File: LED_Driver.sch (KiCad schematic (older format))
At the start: 0 parts

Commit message: Understanding the LED Driver Module
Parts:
- added C? (x2): C, symbol C
- added D?: DIODESCH, symbol DIODESCH
- added L?: INDUCTOR, symbol INDUCTOR
- added R?: R, symbol R
- added U?: AP5726, symbol AP5726
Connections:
- net String+: now also C?.1, D?.2 (K), U?.5 (OVP)
- net String-: now also R?.1, U?.3 (FB)
- new net: D?.1 (A), L?.2, U?.1 (SW)
- new net +5V: C?.1, L?.1, U?.6 (VIN)
- new net GND: C?.2, C?.2, R?.2, U?.2 (GND)
- new net LED_EN_PWM: U?.4 (EN)
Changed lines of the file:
@@
 $Descr A4 11693 8268
 encoding utf-8
-Sheet 6 9
+Sheet 5 9
 Title ""
 Date ""
@@
 Comment4 ""
 $EndDescr
-Text HLabel 2350 2650 0    60   Input ~ 0
-EN
-Text HLabel 2350 3050 0    60   Input ~ 0
-FREQ
-Text HLabel 8650 2650 0    60   Output ~ 0
+Text HLabel 4400 3350 0    60   Input ~ 0
+LED_EN_PWM
+Text HLabel 8500 2100 2    60   Output ~ 0
 String+
-Text HLabel 8650 3000 0    60   Input ~ 0
+Text HLabel 8550 3500 2    60   Input ~ 0
 String-
+$Comp
+L AP5726 U?
+U 1 1 52F43ADC
+P 5400 3350
+F 0 "U?" H 5700 2900 60  0000 C CNN
+F 1 "AP5726" H 5400 3400 60  0000 C CNN
+F 2 "" H 5300 2750 60  0000 C CNN
+F 3 "" H 5300 2750 60  0000 C CNN
+	1    5400 3350
+	1    0    0    -1
+$EndComp
+$Comp
+L +5V #PWR?
+U 1 1 52F43D0D
+P 4550 1950
+F 0 "#PWR?" H 4550 2040 20  0001 C CNN
+F 1 "+5V" H 4550 2040 30  0000 C CNN
+F 2 "" H 4550 1950 60  0000 C CNN
+F 3 "" H 4550 1950 60  0000 C CNN
+	1    4550 1950
+	1    0    0    -1
+$EndComp
+$Comp
+L GND #PWR?
+U 1 1 52F43D24
+P -25900 -92000
+F 0 "#PWR?" H -25900 -92000 30  0001 C CNN
+F 1 "GND" H -25900 -92070 30  0001 C CNN
+F 2 "" H -25900 -92000 60  0000 C CNN
+F 3 "" H -25900 -92000 60  0000 C CNN
+	1    -25900 -92000
+	1    0    0    -1
+$EndComp
+$Comp
+L GND #PWR?
+U 1 1 52F43D42
+P 4550 2800
+F 0 "#PWR?" H 4550 2800 30  0001 C CNN
+F 1 "GND" H 4550 2730 30  0001 C CNN
+F 2 "" H 4550 2800 60  0000 C CNN
+F 3 "" H 4550 2800 60  0000 C CNN
+	1    4550 2800
+	1    0    0    -1
+$EndComp
+$Comp
+L GND #PWR?
+U 1 1 52F43D54
+P 5400 4500
+F 0 "#PWR?" H 5400 4500 30  0001 C CNN
+F 1 "GND" H 5400 4430 30  0001 C CNN
+F 2 "" H 5400 4500 60  0000 C CNN
+F 3 "" H 5400 4500 60  0000 C CNN
+	1    5400 4500
+	1    0    0    -1
+$EndComp
+$Comp
+L C C?
+U 1 1 52F43D64
+P 4550 2400
+F 0 "C?" H 4550 2500 40  0000 L CNN
+F 1 "C" H 4556 2315 40  0000 L CNN
+F 2 "" H 4588 2250 30  0000 C CNN
+F 3 "" H 4550 2400 60  0000 C CNN
+	1    4550 2400
+	1    0    0    -1
+$EndComp
+$Comp
+L C C?
+U 1 1 52F43D9A
+P 7650 2400
+F 0 "C?" H 7650 2500 40  0000 L CNN
+F 1 "C" H 7656 2315 40  0000 L CNN
+F 2 "" H 7688 2250 30  0000 C CNN
+F 3 "" H 7650 2400 60  0000 C CNN
+	1    7650 2400
+	1    0    0    -1
+$EndComp
+$Comp
+L INDUCTOR L?
+U 1 1 52F43DA7
+P 5400 1900
+F 0 "L?" V 5350 1900 40  0000 C CNN
+F 1 "INDUCTOR" V 5500 1900 40  0000 C CNN
+F 2 "" H 5400 1900 60  0000 C CNN
+F 3 "" H 5400 1900 60  0000 C CNN
+	1    5400 1900
+	0    -1   -1   0
+$EndComp
+$Comp
+L DIODESCH D?
+U 1 1 52F43DD1
+P 6050 2100
+F 0 "D?" H 6050 2200 40  0000 C CNN
+F 1 "DIODESCH" H 6050 2000 40  0000 C CNN
+F 2 "" H 6050 2100 60  0000 C CNN
+F 3 "" H 6050 2100 60  0000 C CNN
+	1    6050 2100
+	1    0    0    -1
+$EndComp
+$Comp
+L GND #PWR?
+U 1 1 52F43E01
+P 7650 2800
+F 0 "#PWR?" H 7650 2800 30  0001 C CNN
+F 1 "GND" H 7650 2730 30  0001 C CNN
+F 2 "" H 7650 2800 60  0000 C CNN
+F 3 "" H 7650 2800 60  0000 C CNN
+	1    7650 2800
+	1    0    0    -1
+$EndComp
+$Comp
+L R R?
+U 1 1 52F43E56
+P 6250 3900
+F 0 "R?" V 6330 3900 40  0000 C CNN
+F 1 "R" V 6257 3901 40  0000 C CNN
+F 2 "" V 6180 3900 30  0000 C CNN
+F 3 "" H 6250 3900 30  0000 C CNN
+	1    6250 3900
+	1    0    0    -1
+$EndComp
+Wire Wire Line
+	4400 3350 4650 3350
+Wire Wire Line
+	5400 4500 5400 4050
+Wire Wire Line
+	4550 2800 4550 2600
+Wire Wire Line
+	4550 1950 4550 2200
+Wire Wire Line
+	4550 2100 5250 2100
+Wire Wire Line
+	5250 2100 5250 2650
+Connection ~ 4550 2100
+Wire Wire Line
+	5100 1900 5100 2100
+Connection ~ 5100 2100
+Wire Wire Line
+	5550 2650 5550 2100
+Wire Wire Line
+	5550 2100 5850 2100
+Wire Wire Line
+	5700 2100 5700 1900
+Connection ~ 5700 2100
+Wire Wire Line
+	6250 2100 8500 2100
+Wire Wire Line
+	7650 2100 7650 2200
+Wire Wire Line
+	7650 2800 7650 2600
+Wire Wire Line
+	6100 3200 6350 3200
+Wire Wire Line
+	6350 3200 6350 2100
+Connection ~ 6350 2100
+Connection ~ 7650 2100
+Wire Wire Line
+	6100 3500 8550 3500
+Wire Wire Line
+	6250 3500 6250 3650
+Wire Wire Line
+	6250 4150 6250 4300
+Wire Wire Line
+	6250 4300 5400 4300
+Connection ~ 5400 4300
+Connection ~ 6250 3500
 $EndSCHEMATC

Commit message: Understanding the Arduino Module
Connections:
- net String+ renamed LED_STRING+
- net String- renamed LED_STRING-
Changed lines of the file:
@@
 LIBS:valves
 LIBS:MyComponents
+LIBS:arduino_shieldsNCL
 LIBS:BenchBuddy-cache
 EELAYER 24 0
@@
 LED_EN_PWM
 Text HLabel 8500 2100 2    60   Output ~ 0
-String+
-Text HLabel 8550 3500 2    60   Input ~ 0
-String-
+LED_STRING+
+Text HLabel 8550 3500 2    60   Output ~ 0
+LED_STRING-
 $Comp
 L AP5726 U?

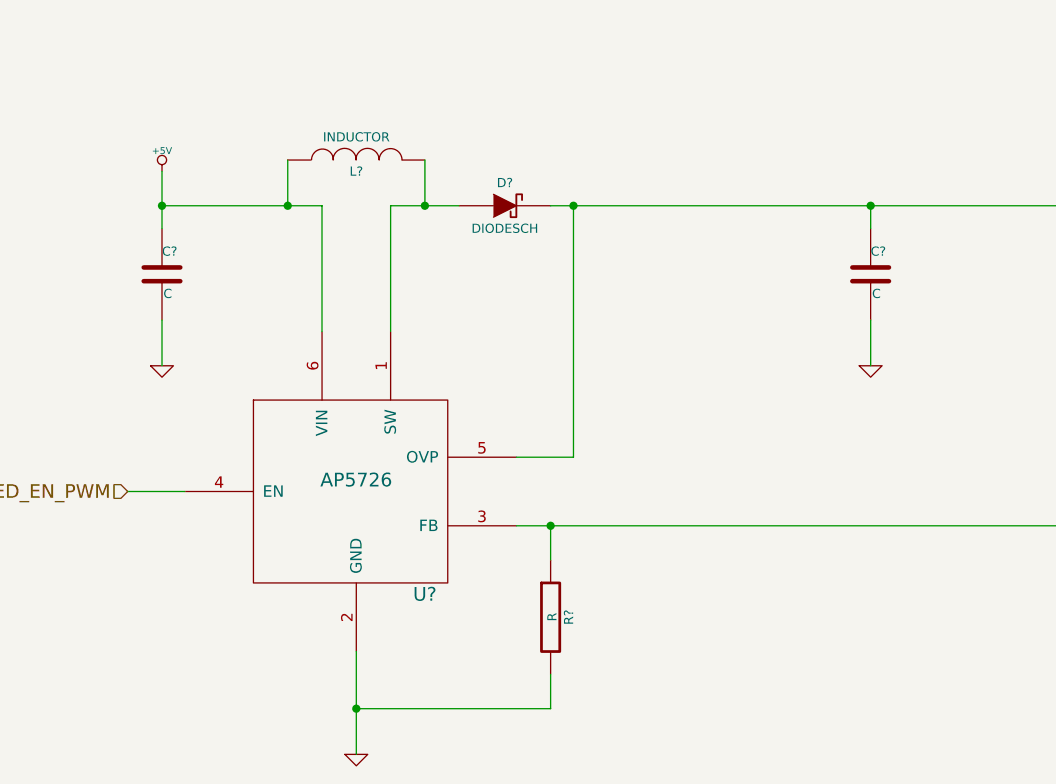
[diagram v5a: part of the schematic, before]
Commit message: Associating and Placing the Relay Module
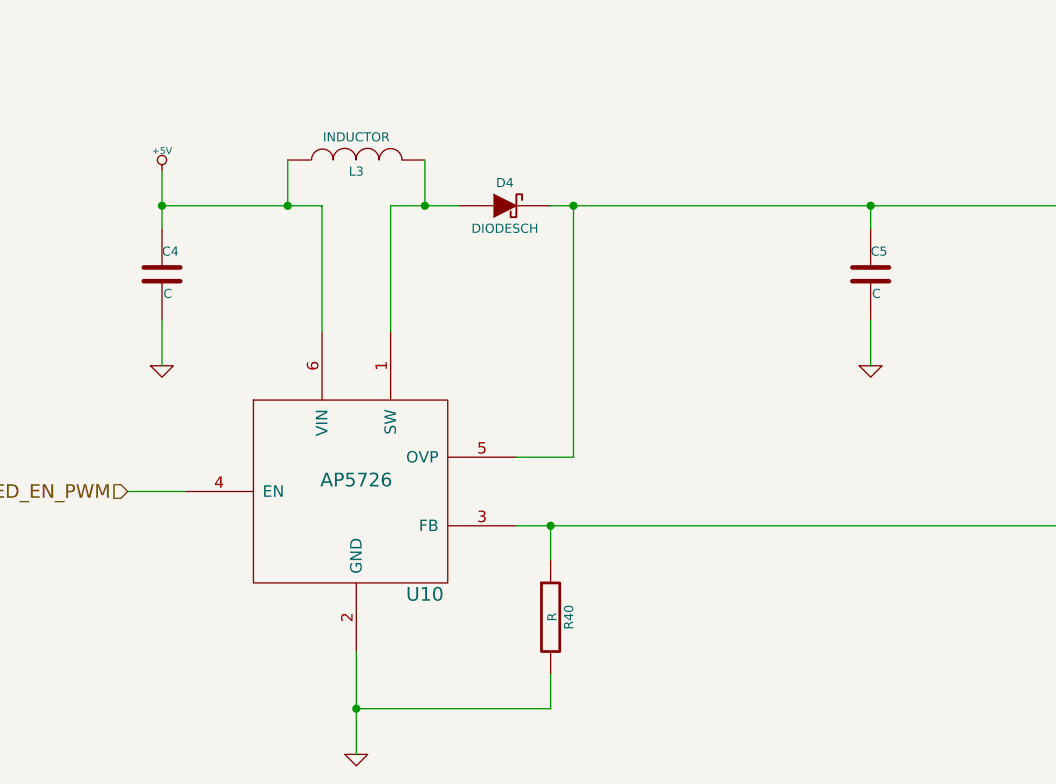
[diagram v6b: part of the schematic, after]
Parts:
- gave numbers to parts that had none: 6
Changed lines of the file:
@@
 LED_STRING-
 $Comp
-L AP5726 U?
+L AP5726 U10
 U 1 1 52F43ADC
 P 5400 3350
-F 0 "U?" H 5700 2900 60  0000 C CNN
+F 0 "U10" H 5700 2900 60  0000 C CNN
 F 1 "AP5726" H 5400 3400 60  0000 C CNN
 F 2 "" H 5300 2750 60  0000 C CNN
@@
 $EndComp
 $Comp
-L +5V #PWR?
+L +5V #PWR046
 U 1 1 52F43D0D
 P 4550 1950
-F 0 "#PWR?" H 4550 2040 20  0001 C CNN
+F 0 "#PWR046" H 4550 2040 20  0001 C CNN
 F 1 "+5V" H 4550 2040 30  0000 C CNN
 F 2 "" H 4550 1950 60  0000 C CNN
@@
 $EndComp
 $Comp
-L GND #PWR?
+L GND #PWR047
 U 1 1 52F43D24
 P -25900 -92000
-F 0 "#PWR?" H -25900 -92000 30  0001 C CNN
+F 0 "#PWR047" H -25900 -92000 30  0001 C CNN
 F 1 "GND" H -25900 -92070 30  0001 C CNN
 F 2 "" H -25900 -92000 60  0000 C CNN
@@
 $EndComp
 $Comp
-L GND #PWR?
+L GND #PWR048
 U 1 1 52F43D42
 P 4550 2800
-F 0 "#PWR?" H 4550 2800 30  0001 C CNN
+F 0 "#PWR048" H 4550 2800 30  0001 C CNN
 F 1 "GND" H 4550 2730 30  0001 C CNN
 F 2 "" H 4550 2800 60  0000 C CNN
@@
 $EndComp
 $Comp
-L GND #PWR?
+L GND #PWR049
 U 1 1 52F43D54
 P 5400 4500
-F 0 "#PWR?" H 5400 4500 30  0001 C CNN
+F 0 "#PWR049" H 5400 4500 30  0001 C CNN
 F 1 "GND" H 5400 4430 30  0001 C CNN
 F 2 "" H 5400 4500 60  0000 C CNN
@@
 $EndComp
 $Comp
-L C C?
+L C C4
 U 1 1 52F43D64
 P 4550 2400
-F 0 "C?" H 4550 2500 40  0000 L CNN
+F 0 "C4" H 4550 2500 40  0000 L CNN
 F 1 "C" H 4556 2315 40  0000 L CNN
 F 2 "" H 4588 2250 30  0000 C CNN
@@
 $EndComp
 $Comp
-L C C?
+L C C5
 U 1 1 52F43D9A
 P 7650 2400
-F 0 "C?" H 7650 2500 40  0000 L CNN
+F 0 "C5" H 7650 2500 40  0000 L CNN
 F 1 "C" H 7656 2315 40  0000 L CNN
 F 2 "" H 7688 2250 30  0000 C CNN
@@
 $EndComp
 $Comp
-L INDUCTOR L?
+L INDUCTOR L3
 U 1 1 52F43DA7
 P 5400 1900
-F 0 "L?" V 5350 1900 40  0000 C CNN
+F 0 "L3" V 5350 1900 40  0000 C CNN
 F 1 "INDUCTOR" V 5500 1900 40  0000 C CNN
 F 2 "" H 5400 1900 60  0000 C CNN
@@
 $EndComp
 $Comp
-L DIODESCH D?
+L DIODESCH D4
 U 1 1 52F43DD1
 P 6050 2100
-F 0 "D?" H 6050 2200 40  0000 C CNN
+F 0 "D4" H 6050 2200 40  0000 C CNN
 F 1 "DIODESCH" H 6050 2000 40  0000 C CNN
 F 2 "" H 6050 2100 60  0000 C CNN
@@
 $EndComp
 $Comp
-L GND #PWR?
+L GND #PWR050
 U 1 1 52F43E01
 P 7650 2800
-F 0 "#PWR?" H 7650 2800 30  0001 C CNN
+F 0 "#PWR050" H 7650 2800 30  0001 C CNN
 F 1 "GND" H 7650 2730 30  0001 C CNN
 F 2 "" H 7650 2800 60  0000 C CNN
@@
 $EndComp
 $Comp
-L R R?
+L R R40
 U 1 1 52F43E56
 P 6250 3900
-F 0 "R?" V 6330 3900 40  0000 C CNN
+F 0 "R40" V 6330 3900 40  0000 C CNN
 F 1 "R" V 6257 3901 40  0000 C CNN
 F 2 "" V 6180 3900 30  0000 C CNN
